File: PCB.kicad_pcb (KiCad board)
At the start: 2 copper layers, 60 x 60 mm, 54 parts, among them J1 USB_C_Receptacle_USB2.0_16P, J10 Conn_01x05_Pin, J11 Conn_01x05_Pin, J12 Conn_01x03_Pin, J3 Conn_01x04_Pin, J5 Conn_01x02_Pin, J6 Conn_01x02_Pin, J7 Conn_01x02_Pin, J8 Conn_01x04_Pin, SW1 SW_Push, SW2 SW_Push, U1 TMC2209_SILENTSTEPSTICK, U3 D3V3XA4B10LP, U4 AMS1117-3.3 (UMW), U5 TMC2209_SILENTSTEPSTICK, U6 ESP32-S3-WROOM-1

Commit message: debut V3
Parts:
- removed BZ1: Buzzer, Buzzer_Beeper:Buzzer_12x9.5RM7.6
- removed G***: LOGO, Tux:tux2
- removed J10, J11: Conn_01x05_Pin, Connector_PinHeader_2.54mm:PinHeader_1x05_P2.54mm_Vertical
- removed J12: Conn_01x03_Pin, Connector_PinHeader_2.54mm:PinHeader_1x03_P2.54mm_Vertical
- removed JP5, JP6: Jumper_2_Open, Connector_PinHeader_2.54mm:PinHeader_1x02_P2.54mm_Vertical
- removed JP7, JP8: Jumper_2_Open, Resistor_SMD:R_1206_3216Metric_Pad1.30x1.75mm_HandSolder
- removed S1, S2, S3, S4, S5, S6, S7: Conn_01x07_Pin, Connector_PinHeader_2.54mm:PinHeader_1x03_P2.54mm_Vertical
- removed SCREEN, TOF: Conn_01x04_Pin, Connector_PinHeader_2.54mm:PinHeader_1x04_P2.54mm_Vertical
- removed U3: D3V3XA4B10LP, Package_DFN_QFN:Diodes_UDFN-10_1.0x2.5mm_P0.5mm
- added F1: Fuse, Fuse:Fuse_1206_3216Metric, F.Cu at (160.0, 118.2)
- added J13: Conn_01x06_Pin, Connector_PinHeader_2.54mm:PinHeader_1x06_P2.54mm_Vertical, F.Cu at (115.5, 108.3)
- added J4: Conn_01x06_Pin, Connector_PinHeader_2.54mm:PinHeader_1x06_P2.54mm_Vertical, F.Cu at (120.6, 108.3)
- added J9: Conn_01x06_Pin, Connector_PinHeader_2.54mm:PinHeader_1x06_P2.54mm_Vertical, F.Cu at (118.1, 108.3)
- added JP3: Jumper_2_Open, Connector_PinHeader_2.54mm:PinHeader_1x02_P2.54mm_Vertical, F.Cu at (154.7, 88.5)
- added JP4: Jumper_2_Open, Connector_PinHeader_2.54mm:PinHeader_1x02_P2.54mm_Vertical, F.Cu at (157.2, 88.5)
- added R6: 10k, Resistor_SMD:R_1206_3216Metric_Pad1.30x1.75mm_HandSolder, F.Cu at (124.2, 129.4)
- added R7: 120, Resistor_SMD:R_0805_2012Metric_Pad1.20x1.40mm_HandSolder, F.Cu at (125.0, 105.4)
- added R8: 120, Resistor_SMD:R_0805_2012Metric_Pad1.20x1.40mm_HandSolder, F.Cu at (125.0, 103.2)
- added R9: 120, Resistor_SMD:R_0805_2012Metric_Pad1.20x1.40mm_HandSolder, F.Cu at (125.0, 101.0)
- added SCREEN2: Conn_01x04_Pin, Connector_PinHeader_2.54mm:PinHeader_1x04_P2.54mm_Vertical, F.Cu at (146.8, 106.5)
- added TOF2: Conn_01x04_Pin, Connector_PinHeader_2.54mm:PinHeader_1x04_P2.54mm_Vertical, F.Cu at (139.4, 73.6)
- added U2: USBLC6-2SC6, Package_TO_SOT_SMD:SOT-23-6_Handsoldering, F.Cu at (159.9, 114.5)
- added UART1: Conn_01x04_Pin, Connector_PinHeader_2.54mm:PinHeader_1x04_P2.54mm_Vertical, F.Cu at (154.1, 97.8)
- D2: value ~ -> SMLVN6RGB; footprint LED_SMD:LED_0805_2012Metric_Pad1.15x1.40mm_HandSolder -> LED_SMD:LED_RGB_5050-6
- H1, H2, H3, H4: value MountingHole -> MountingHole_Pad; footprint MountingHole:MountingHole_3.2mm_M3 -> MountingHole:MountingHole_3.2mm_M3_Pad
- R5: value 120 -> 10k; footprint Resistor_SMD:R_0805_2012Metric_Pad1.20x1.40mm_HandSolder -> Resistor_SMD:R_1206_3216Metric_Pad1.30x1.75mm_HandSolder
- moved H3 56.6 mm to (169.8, 128.0)
- moved H1 56.6 mm to (169.8, 75.0)
- moved J7 53.5 mm to (126.2, 73.8), turned to -90 degrees
- moved H4 50.4 mm to (116.8, 128.0)
- moved H2 50.4 mm to (116.8, 75.0)
- moved UART0 49.0 mm to (125.0, 78.0)
- moved D2 46.1 mm to (118.0, 101.2), turned to 180 degrees
- moved J5 45.3 mm to (160.7, 73.8), turned to 90 degrees
- moved R5 33.0 mm to (124.2, 126.6), turned to 0 degrees
- moved D1 29.8 mm to (166.4, 97.6), turned to 180 degrees
- moved R4 27.6 mm to (171.0, 97.6), turned to 0 degrees
- moved C8 23.2 mm to (171.2, 90.5), turned to 90 degrees
- moved J6 22.8 mm to (158.8, 104.1), turned to 0 degrees
- moved J3 20.3 mm to (161.8, 78.0)
- moved C3 11.9 mm to (115.5, 85.3), turned to -90 degrees
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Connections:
- net GPIO0 renamed BOOT
- D2 pad 1: Net-(D2-K) -> Net-(D2-BA)
- D2 pad 2: LED -> Net-(D2-RA)
- J1 pad A6: USB_P -> USB_P_in
- J1 pad A7: USB_N -> USB_N_in
- J1 pad B6: USB_P -> USB_P_in
- J1 pad B7: USB_N -> USB_N_in
- J6 pad 2: VCC_5Vin -> VCC_5Vout
- R5 pad 1: Net-(D2-K) -> VCC_5V
- R5 pad 2: GND -> SCL
- U6 pad 19: STEP2 -> GPIO11_PWM
- U6 pad 20: GPIO12 -> GPIO12_PWM
- U6 pad 21: STEP1 -> GPIO13_PWM
- U6 pad 22: DIR1 -> GPIO14_PWM
- U6 pad 28: GPIO35 -> STEP1
- U6 pad 29: GPIO36 -> DIR1
- U6 pad 30: GPIO37 -> STEP2
- U6 pad 31: GPIO38 -> DIR2
- U6 pad 4: LED -> GPIO4
- U6 pad 5: BUZZER -> GPIO5
- U6 pad 8: DIR2 -> GPIO15_PWM
- U6 pad 9: unconnected-(U6-IO16-Pad9) -> GPIO16_PWM
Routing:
- net VCC_5V: track 344.8 -> 0.00 mm, vias 8 -> 0
- net GND: track 107.2 -> 0.00 mm, vias 129 -> 0
- net 3V3: track 76.2 -> 0.00 mm, vias 1 -> 0
- net SDA: track 67.2 -> 0.00 mm, vias 6 -> 0
- net SCL: track 66.0 -> 0.00 mm, vias 4 -> 0
- net STEP2: track 63.3 -> 0.00 mm
- net DIR2: track 55.7 -> 0.00 mm
- net MOTORA2: track 53.4 -> 0.00 mm
- net DIR1: track 44.1 -> 0.00 mm
- net STEP1: track 44.0 -> 0.00 mm, vias 2 -> 0
- net MOTORA1: track 43.2 -> 0.00 mm
- net MOTORC1: track 42.6 -> 0.00 mm
- net MOTORC2: track 35.4 -> 0.00 mm
- net MOTORA3: track 28.8 -> 0.00 mm
- net MOTORC3: track 28.2 -> 0.00 mm
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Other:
- outline, holes or cut-outs redrawn
- board text added: "BT1"
- board text added: "BT2"
- board text added: "MS1"
- board text added: "MS2"
- board text added: "RGB"
- board text added: "SCREEN"
- board text added: "TOF"
- board text removed: "+"
- board text removed: "-"
- board text removed: "1"
- board text removed: "16"
- board text removed: "2"
- board text removed: "2025 V.2"
- board text removed: "21"
- board text removed: "32"
- board text removed: "35"
- board text removed: "36"
- board text removed: "37"
- board text removed: "38"
- board text removed: "3V3"
- board text removed: "47"
- board text removed: "48"
- board text removed: "5V"
- board text removed: "64"
- board text removed: "8"
- board text removed: "<3"
- board text removed: "BAU"
- board text removed: "BOOT"
- board text removed: "BTN"
- board text removed: "DRIVER1"
- board text removed: "DRIVER2"
- board text removed: "GND"
- board text removed: "I²C"
- board text removed: "M0"
- board text removed: "M1"
- board text removed: "RATP"
- board text removed: "RST"
- board text removed: "RX"
- board text removed: "SCL"
- board text removed: "SDA"
- board text removed: "Servomotors"
- board text removed: "TX"
- board text removed: "UART0"
- board text removed: "Unimakers"
- board text removed: "VCC"
- board text removed: "step"

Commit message: fin du routage
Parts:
- removed TOF2: Conn_01x04_Pin, Connector_PinHeader_2.54mm:PinHeader_1x04_P2.54mm_Vertical
- added J2: Conn_01x06_Socket, Connector_PinSocket_2.54mm:PinSocket_1x06_P2.54mm_Vertical, F.Cu at (136.8, 73.6)
- C1, C10, C2, C9: footprint Resistor_SMD:R_0805_2012Metric_Pad1.20x1.40mm_HandSolder -> Capacitor_SMD:C_0805_2012Metric_Pad1.18x1.45mm_HandSolder
- SCREEN2: footprint Connector_PinHeader_2.54mm:PinHeader_1x04_P2.54mm_Vertical -> Connector_PinSocket_2.54mm:PinSocket_1x04_P2.54mm_Vertical
- moved C1 9.65 mm to (121.8, 129.2), turned to 90 degrees
- moved R3 8.01 mm to (159.6, 113.2)
- moved C9 5.99 mm to (158.8, 126.0), turned to 180 degrees
- moved C2 5.85 mm to (164.4, 129.4)
- moved SW2 4.91 mm to (160.0, 129.5), turned to 180 degrees
- moved R6 4.29 mm to (126.2, 125.6)
- moved R5 4.29 mm to (126.2, 122.8)
- moved SW1 3.79 mm to (126.2, 129.3), turned to 180 degrees
- moved C10 3.28 mm to (163.4, 126.0), turned to 0 degrees
- moved JP2 2.66 mm to (129.5, 87.2)
- moved U2 2.45 mm to (158.6, 116.6)
- moved JP1 2.42 mm to (132.1, 87.2)
- moved F1 2.01 mm to (159.8, 120.2)
- moved SCREEN2 1.41 mm to (146.9, 105.1)
- moved R1 0.80 mm to (160.0, 123.2)
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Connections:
- net RX0 renamed UART0-
- net RX1 renamed UART1-
- net TX0 renamed UART0+
- net TX1 renamed UART1+
- J1 pad A6: USB_P_in -> in_USB_P
- J1 pad A7: USB_N_in -> in_USB_N
- J1 pad B6: USB_P_in -> in_USB_P
- J1 pad B7: USB_N_in -> in_USB_N
- R5 pad 1: VCC_5V -> 3V3
- R6 pad 1: VCC_5V -> 3V3
- U2 pad 1: USB_P_in -> in_USB_N
- U2 pad 3: USB_N_in -> in_USB_P
- U2 pad 4: USB_N -> USB_P
- U2 pad 6: USB_P -> USB_N
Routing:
- net VCC_5V: track 0.00 -> 202.3 mm, vias 0 -> 1
- net GND: track 0.00 -> 104.9 mm, vias 0 -> 78
- net 3V3: track 0.00 -> 90.0 mm, vias 0 -> 2
- net SDA: track 0.00 -> 85.2 mm, vias 0 -> 2
- net SCL: track 0.00 -> 76.2 mm, vias 0 -> 1
- net LAUNCHPULL: track 0.00 -> 71.1 mm, vias 0 -> 4
- net UART0-: track 0.00 -> 63.3 mm
- net UART0+: track 0.00 -> 62.5 mm
- net TEAMBTN: track 0.00 -> 58.9 mm, vias 0 -> 5
- net DIR2: track 0.00 -> 51.6 mm, vias 0 -> 2
- net GPIO15_PWM: track 0.00 -> 48.6 mm, vias 0 -> 2
- net DIR1: track 0.00 -> 47.3 mm, vias 0 -> 4
- net STEP2: track 0.00 -> 45.7 mm, vias 0 -> 2
- net STEP1: track 0.00 -> 44.5 mm, vias 0 -> 4
- net GPIO14_PWM: track 0.00 -> 38.4 mm, vias 0 -> 2
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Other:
- outline, holes or cut-outs redrawn

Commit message: serigraphie
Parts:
- added SW3: SW_DIP_x04, Button_Switch_THT:SW_DIP_SPSTx04_Slide_9.78x12.34mm_W7.62mm_P2.54mm, F.Cu at (1.44, 2.73)
- moved J6 0.60 mm to (159.4, 104.1)
- moved C2 0.20 mm to (164.4, 129.2)
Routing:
- net DIR2: track 51.6 -> 48.9 mm
- net SDA: track 85.2 -> 83.6 mm
- net SCL: track 76.2 -> 75.1 mm
- net GPIO13_PWM: track 25.2 -> 24.3 mm
- net GPIO15_PWM: track 48.6 -> 48.1 mm
- net GND: vias 78 -> 79
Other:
- outline, holes or cut-outs redrawn
- board text added: "+"
- board text added: "-"
- board text added: "11"
- board text added: "12"
- board text added: "13"
- board text added: "14"
- board text added: "15"
- board text added: "16"
- board text added: "21"
- board text added: "5"
- board text added: "5V"
- board text added: "6"
- board text added: "7"
- board text added: "9"
- board text added: ">"
- board text added: "AMS1117 3.3"
- board text added: "BTN"
- board text added: "C0.1uF"
- board text added: "C10uF"
- board text added: "E-STOP"
- board text added: "ESD"
- board text added: "FUSE"
- board text added: "GND"
- board text added: "Good Luck ;)"
- board text added: "MOTOR 1"
- board text added: "MOTOR 2"
- board text added: "PWM PWM PWM F0 F0 F0"
- board text added: "R10k"
- board text added: "R120"
- board text added: "R5.1k"
- board text added: "RATP 2025 - V3"
- board text added: "RX"
- board text added: "S"
- board text added: "SCL"
- board text added: "SDA"
- board text added: "SERVOMOTORS"
- board text added: "TX"
- board text added: "Type-C"

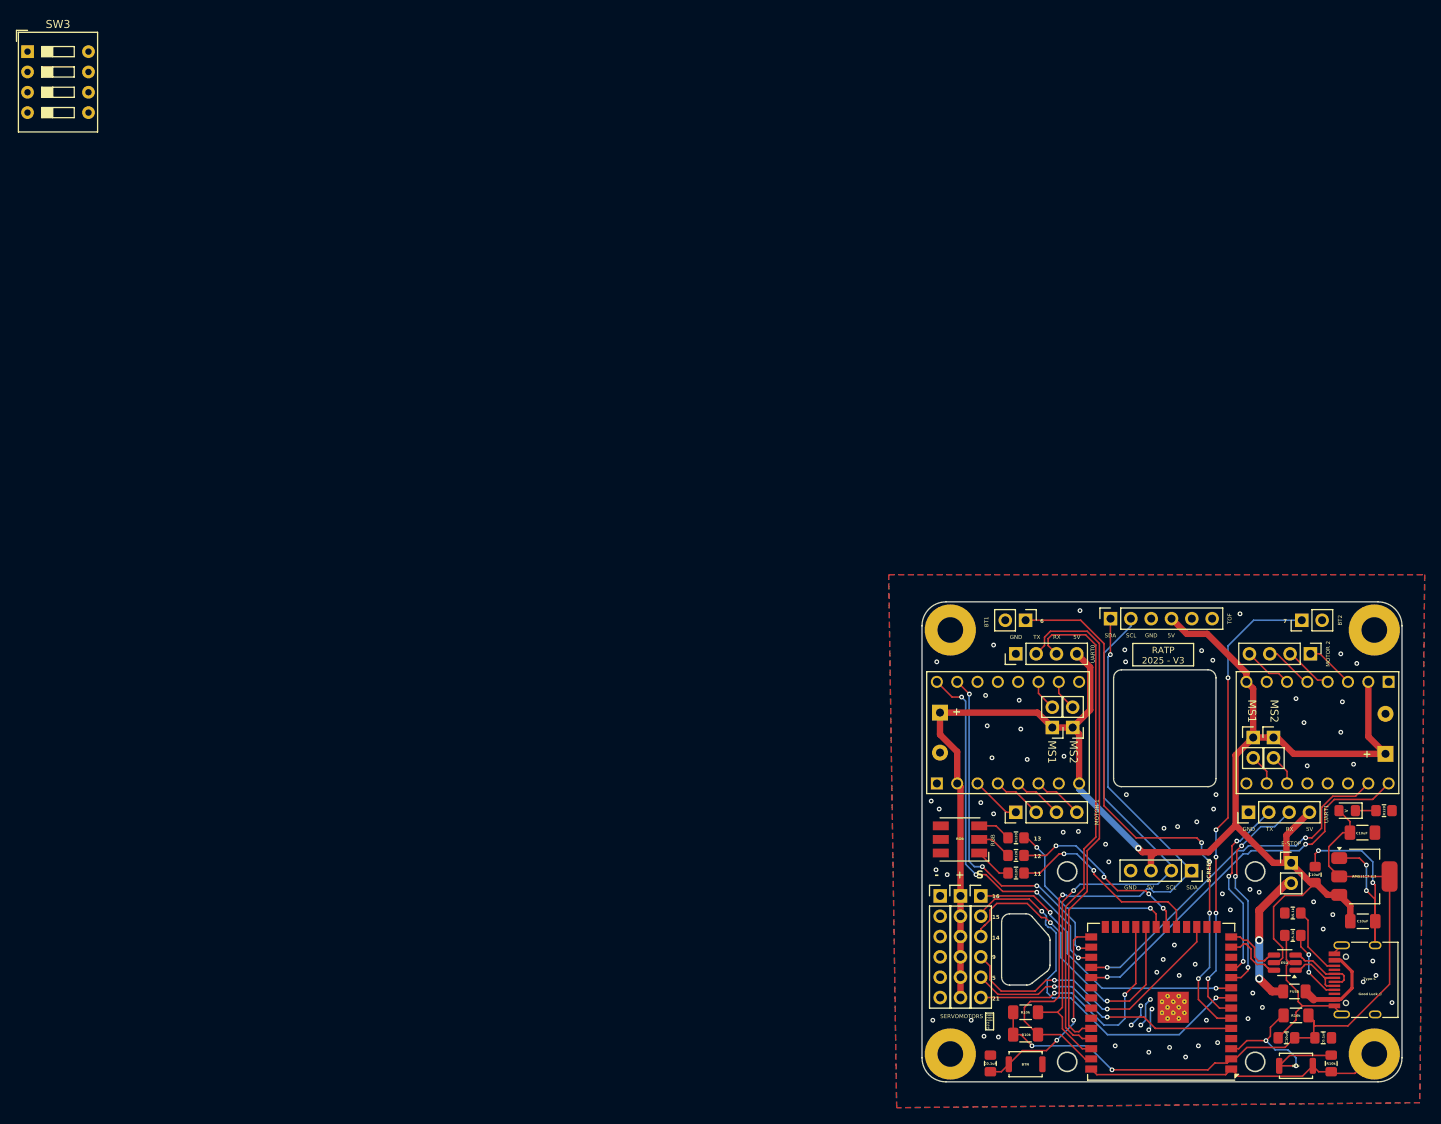
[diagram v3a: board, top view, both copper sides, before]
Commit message: ajout largeur piste + fix erreurs (DRC NOK)
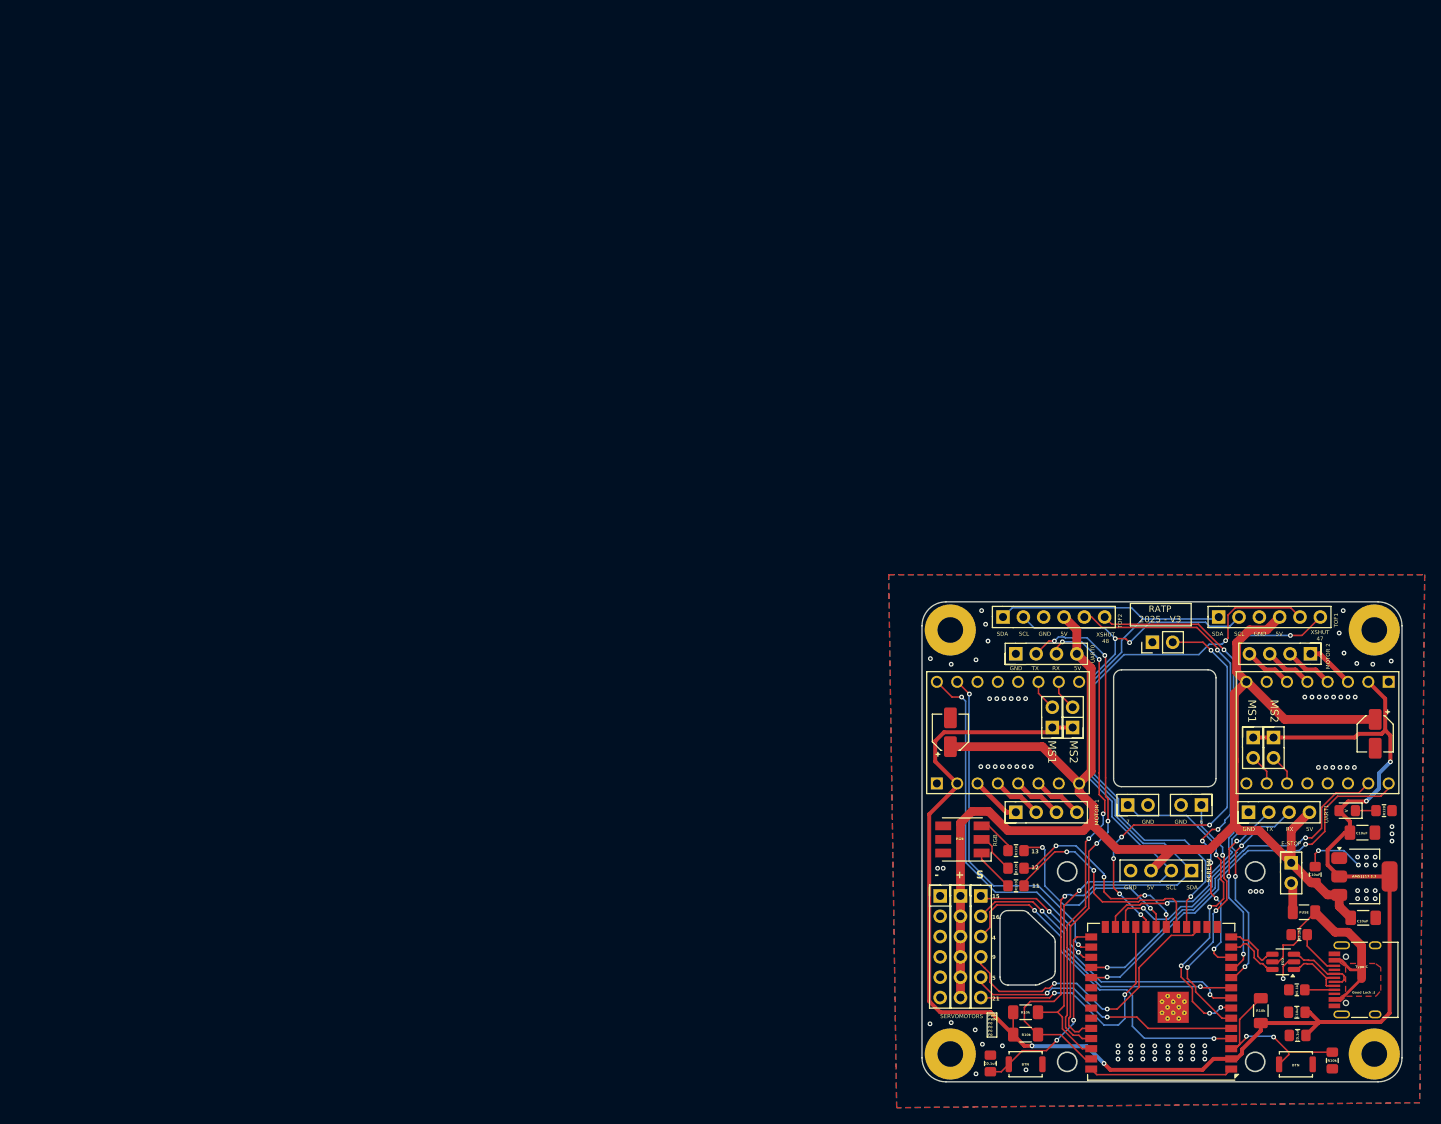
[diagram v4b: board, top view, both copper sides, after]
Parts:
- removed SW3: SW_DIP_x04, Button_Switch_THT:SW_DIP_SPSTx04_Slide_9.78x12.34mm_W7.62mm_P2.54mm
- added J10: Conn_01x06_Socket, Connector_PinSocket_2.54mm:PinSocket_1x06_P2.54mm_Vertical, F.Cu at (123.4, 73.4)
- added J11: Conn_01x02_Pin, Connector_PinHeader_2.54mm:PinHeader_1x02_P2.54mm_Vertical, F.Cu at (142.1, 76.5)
- C3, C8: footprint Capacitor_THT:CP_Radial_D10.0mm_P5.00mm -> Capacitor_SMD:CP_Elec_4x5.7
- moved J7 31.9 mm to (148.2, 96.9)
- moved J5 31.7 mm to (139.0, 96.9)
- moved J2 13.5 mm to (150.3, 73.4)
- moved F1 9.97 mm to (161.0, 110.3)
- moved R3 6.82 mm to (160.1, 120.0)
- moved R1 4.44 mm to (155.6, 122.6), turned to 90 degrees
- moved C9 3.45 mm to (160.1, 122.8)
- moved C10 3.21 mm to (160.2, 125.7), turned to 180 degrees
- moved R2 2.82 mm to (160.4, 113.1)
- moved C8 2.81 mm to (169.9, 88.0), turned to -90 degrees
- moved C3 2.77 mm to (116.8, 87.8), turned to 90 degrees
- moved R7 1.60 mm to (125.0, 107.0)
- moved R8 1.60 mm to (125.0, 104.8)
- moved R9 1.60 mm to (125.0, 102.6)
- moved C5 0.43 mm to (168.4, 111.0)
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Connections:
- J2 pad 5: unconnected-(J2-Pin_5-Pad5) -> GPIO10
- J2 pad 6: unconnected-(J2-Pin_6-Pad6) -> XSHUT1
- J4 pad 1: GPIO16_PWM -> GPIO15_PWM
- J4 pad 2: GPIO15_PWM -> GPIO16_PWM
- J4 pad 3: GPIO14_PWM -> GPIO4
- JP1 pad 1: VCC_5V -> 3V3
- JP2 pad 1: VCC_5V -> 3V3
- JP3 pad 1: VCC_5V -> 3V3
- JP4 pad 1: VCC_5V -> 3V3
- U1 pad 2: VCC_5V -> 3V3
- U2 pad 5: VCC_5V -> VCC_5Vin
- U5 pad 2: VCC_5V -> 3V3
- U6 pad 24: GPIO47 -> XSHUT1
- U6 pad 25: GPIO48 -> XSHUT2
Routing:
- net 3V3: track 90.0 -> 198.2 mm, vias 2 -> 4
- net GND: track 104.9 -> 29.4 mm, vias 79 -> 93
- net GPIO10: track 0.00 -> 71.9 mm, vias 0 -> 2
- net XSHUT2: track 0.00 -> 62.8 mm, vias 0 -> 2
- net GPIO8: track 0.00 -> 62.6 mm, vias 0 -> 6
- net XSHUT1: track 0.00 -> 59.4 mm, vias 0 -> 2
- net GPIO4: track 0.00 -> 44.3 mm, vias 0 -> 2
- net LAUNCHPULL: track 71.1 -> 33.0 mm, vias 4 -> 3
- net SDA: track 83.6 -> 116.0 mm, vias 2 -> 1
- net SCL: track 75.1 -> 103.4 mm, vias 1 -> 3
- net VCC_5Vin: track 11.7 -> 29.2 mm
- net TEAMBTN: track 58.9 -> 42.2 mm
- net GPIO14_PWM: track 38.5 -> 53.9 mm, vias 2 -> 6
- net VCC_5Vout: track 17.0 -> 3.72 mm, vias 2 -> 0
- net VCC_5V: track 202.2 -> 192.1 mm, vias 1 -> 0
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- added copper zone on F.Cu, net VCC_5Vin
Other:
- outline, holes or cut-outs redrawn
- board text added: "4"
- board text added: "PWM PWM F0 F0 F0 F0"
- board text added: "TOF1"
- board text added: "TOF2"
- board text added: "XSHUT 47"
- board text added: "XSHUT 48"
- board text removed: "14"
- board text removed: "BT1"
- board text removed: "BT2"
- board text removed: "PWM PWM PWM F0 F0 F0"
- board text removed: "TOF"
